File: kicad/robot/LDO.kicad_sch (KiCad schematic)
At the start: 17 parts, among them U14 MAX77642ANA+

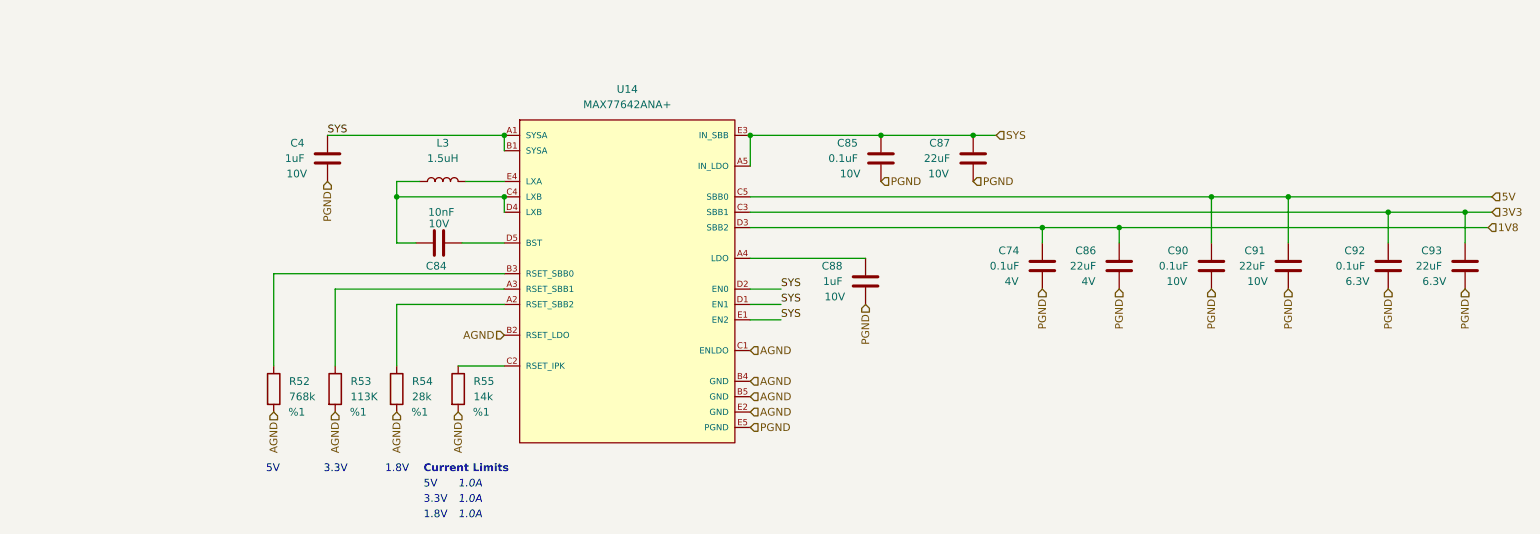
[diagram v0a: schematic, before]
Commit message: Add current breaks between each section of hardware.
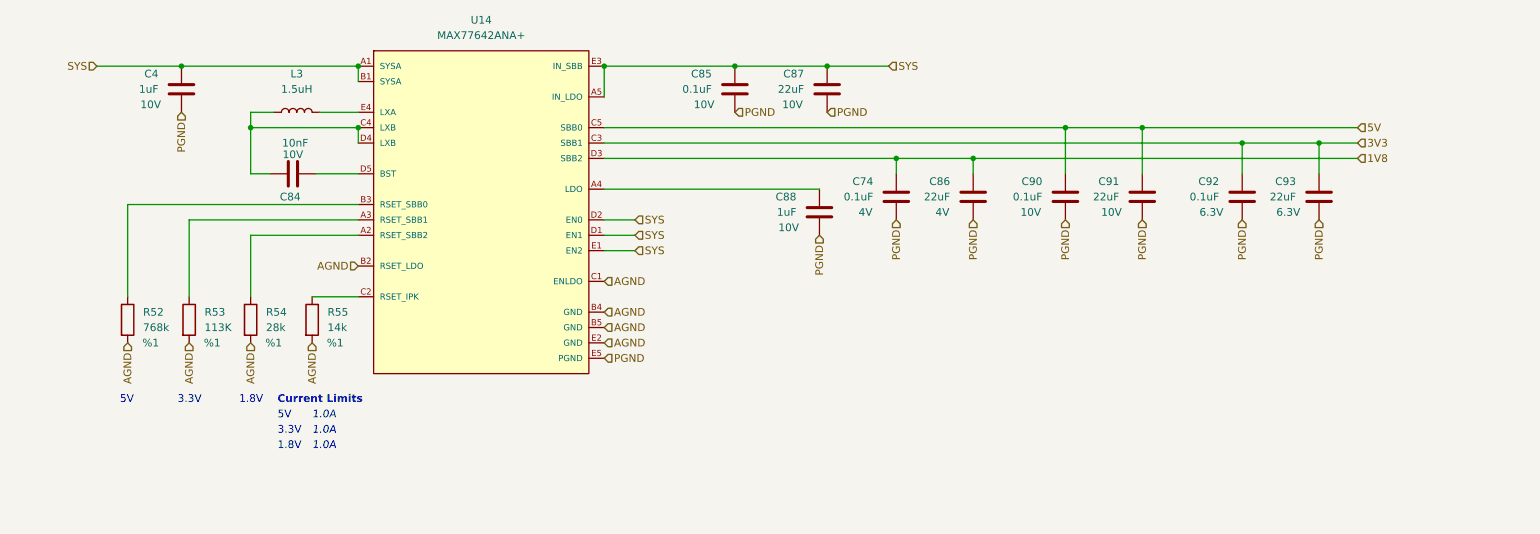
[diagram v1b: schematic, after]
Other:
- moved on the sheet: C4, C74, C84, C85, C86, C87, C88, C90, C91, C92, C93, L3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

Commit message: Add test points for testing current on SIMO. Also add shunt switches to turn on/off each (i.e. on pins D2, D1, and E1).
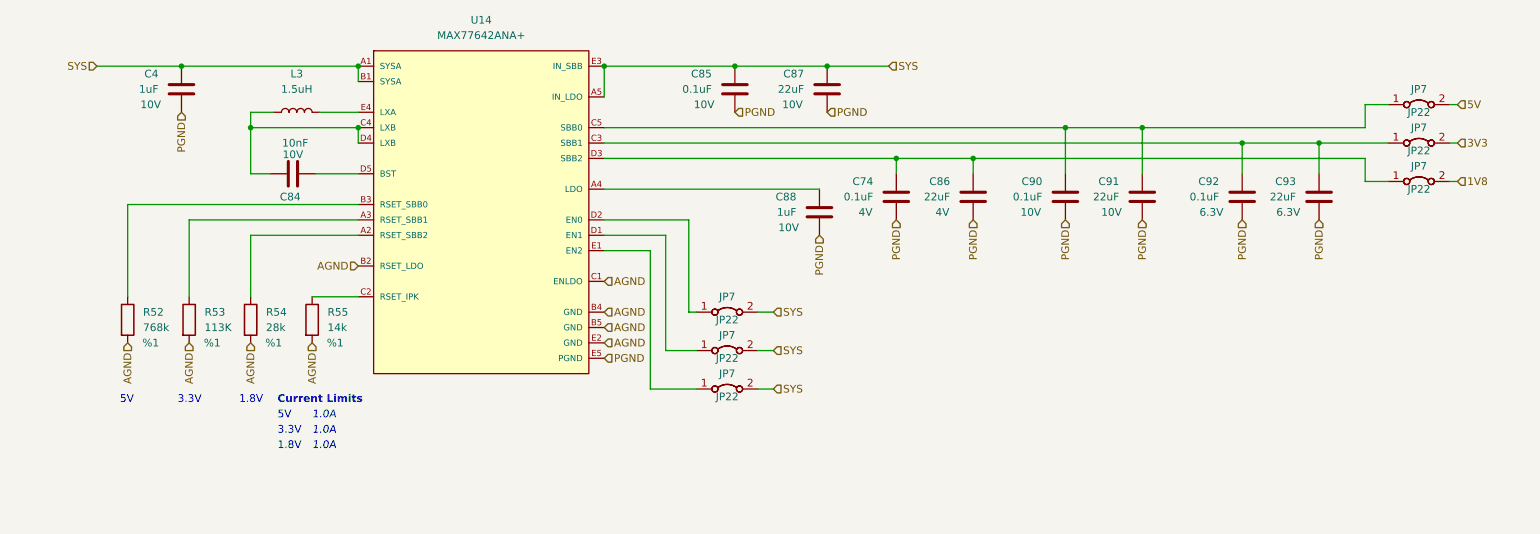
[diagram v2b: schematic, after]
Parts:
- added JP22 (x6): Jumper, custom_connectors:2.54mm_2pointJumper, symbol Jumper:Jumper
- added JP7 (x6): Jumper_Bridged, custom_connectors:2.54mm_2pointJumperClosed, symbol Jumper:Jumper_2_Bridged
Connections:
- net 1V8: now also JP7.2 (B); no longer C74.1, C86.1, U14.D3 (SBB2)
- net 3V3: now also JP7.2 (B); no longer C92.1, C93.1, U14.C3 (SBB1)
- net 5V: now also JP7.2 (B); no longer C90.1, C91.1, U14.C5 (SBB0)
- net SYS: now also JP7.2 (B), JP7.2 (B), JP7.2 (B); no longer U14.D1 (EN1), U14.D2 (EN0), U14.E1 (EN2)
- new net: C92.1, C93.1, JP7.1 (A), U14.C3 (SBB1)
- new net: C74.1, C86.1, JP7.1 (A), U14.D3 (SBB2)
- new net: C90.1, C91.1, JP7.1 (A), U14.C5 (SBB0)
- new net: JP7.1 (A), U14.D1 (EN1)
- new net: JP7.1 (A), U14.D2 (EN0)
- new net: JP7.1 (A), U14.E1 (EN2)

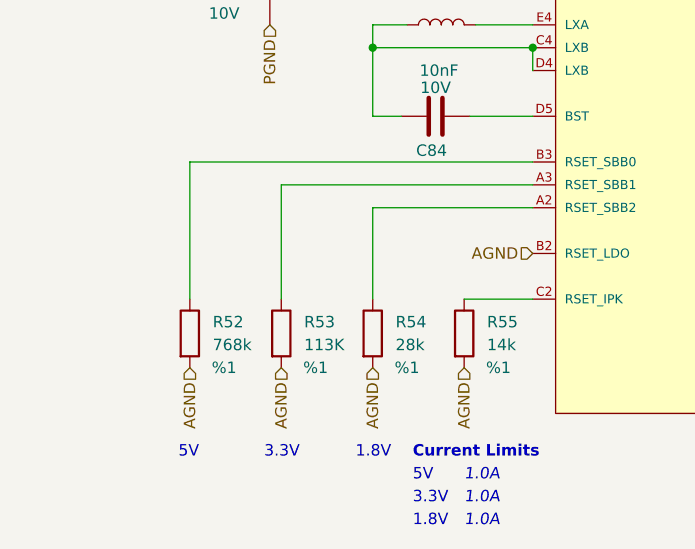
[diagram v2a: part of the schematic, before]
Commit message: Added set resistor for LDO and changed size to 0603 for LDO output capacitor as recommended by datasheet Output Capacitor Selection
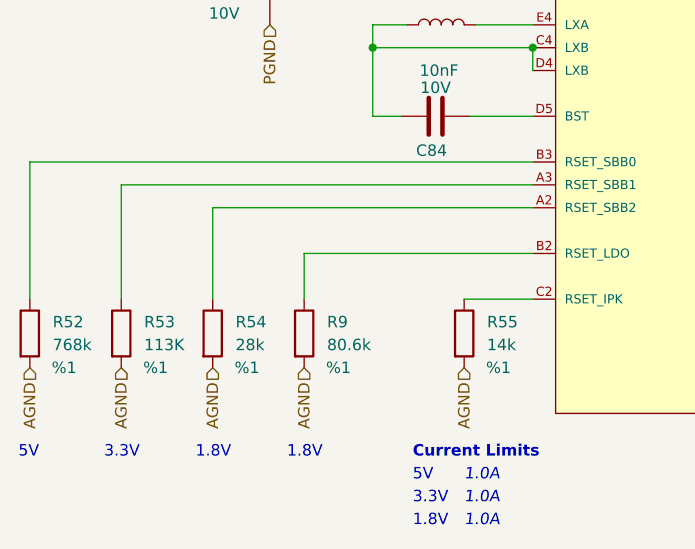
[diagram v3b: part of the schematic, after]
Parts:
- added R9: 80.6k, Resistor_SMD:R_0402_1005Metric, symbol Device:R
- C88: footprint Capacitor_SMD:C_0402_1005Metric -> Capacitor_SMD:C_0603_1608Metric; Manufacturer Murata -> (none); Part Number GRM155R61E105KA12D -> (none)
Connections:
- net AGND: now also R9.2; no longer U14.B2 (RSET_LDO)
- new net: R9.1, U14.B2 (RSET_LDO)
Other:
- moved on the sheet: R52, R53, R54

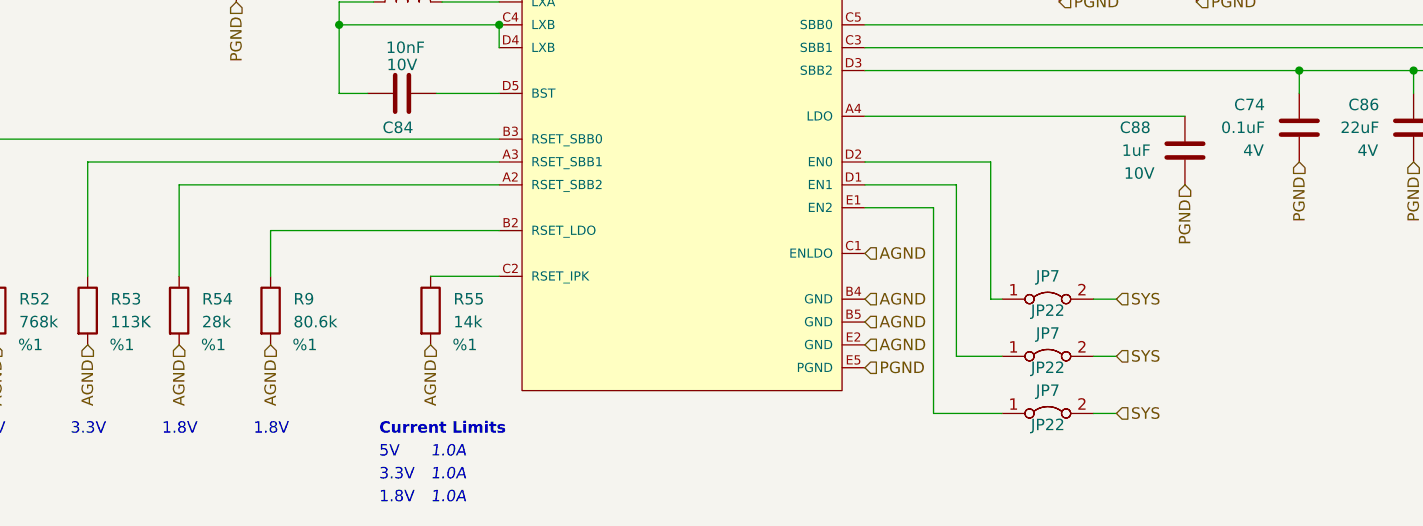
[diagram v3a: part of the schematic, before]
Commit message: Enable LDO and set it at 1.8V and Disable SBB2 and follow recommendations for unused outputs
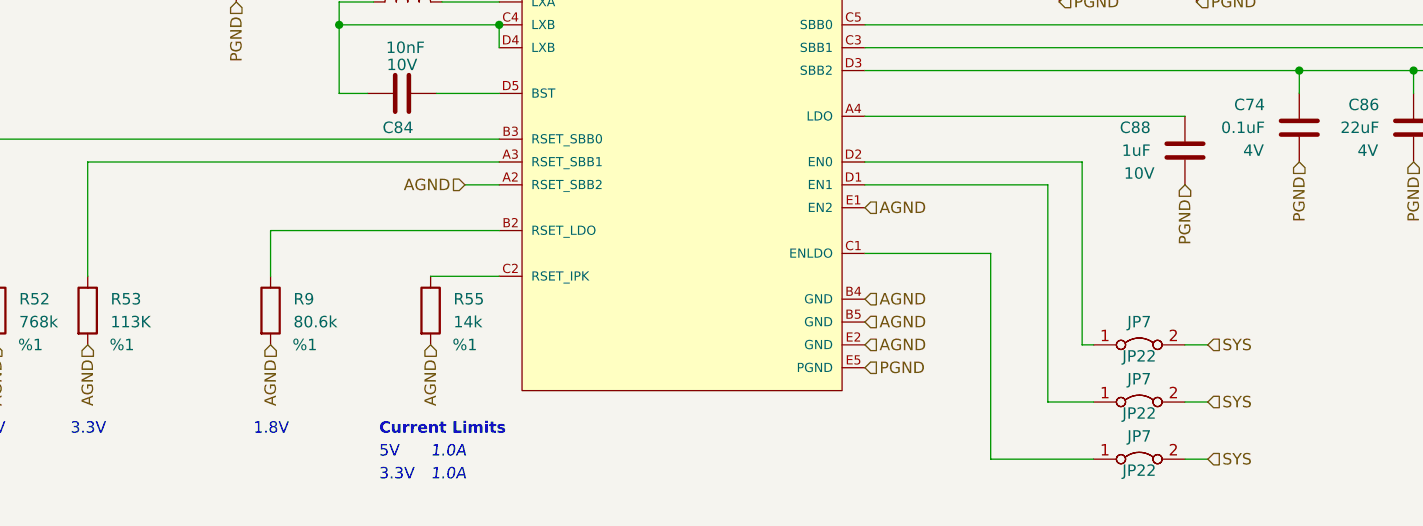
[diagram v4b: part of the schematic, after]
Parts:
- removed R54: 28k, Resistor_SMD:R_0603_1608Metric, symbol Device:R
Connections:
- net AGND: now also U14.A2 (RSET_SBB2), U14.E1 (EN2); no longer U14.C1 (ENLDO)
- net at JP7.1 (A): now also U14.C1 (ENLDO); no longer U14.E1 (EN2)
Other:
- moved on the sheet: JP22, JP7

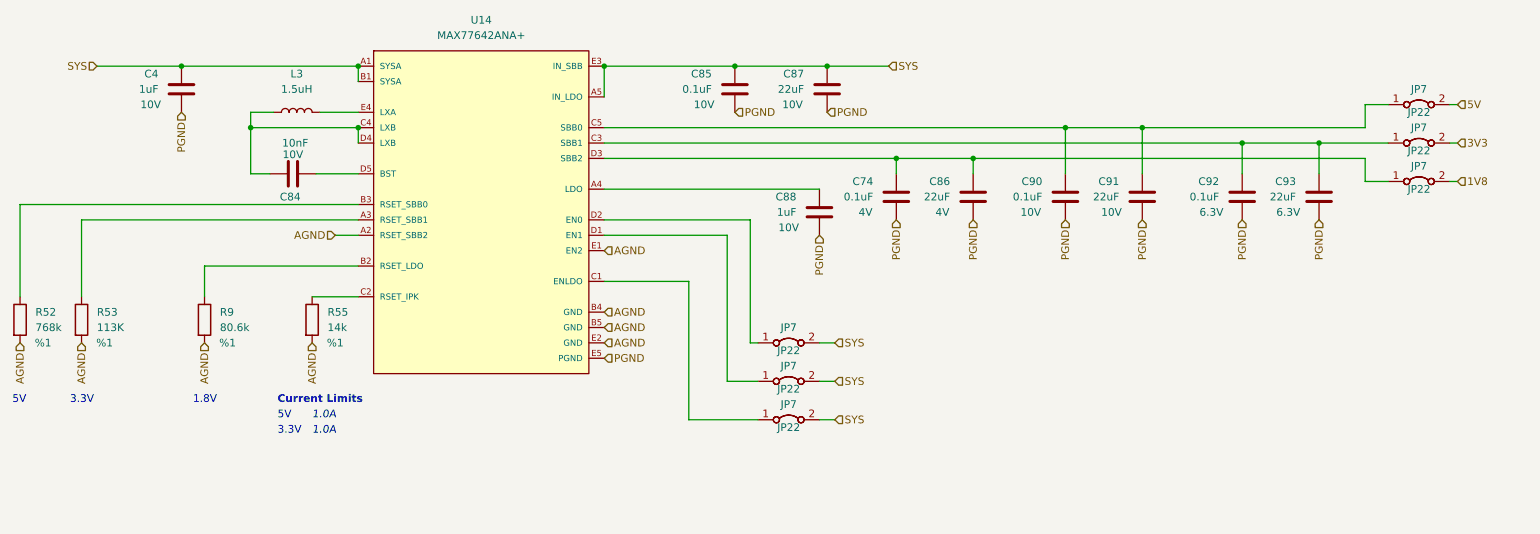
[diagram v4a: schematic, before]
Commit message: Eleminated 5V rail and corrected a few mistakes in SIMO config
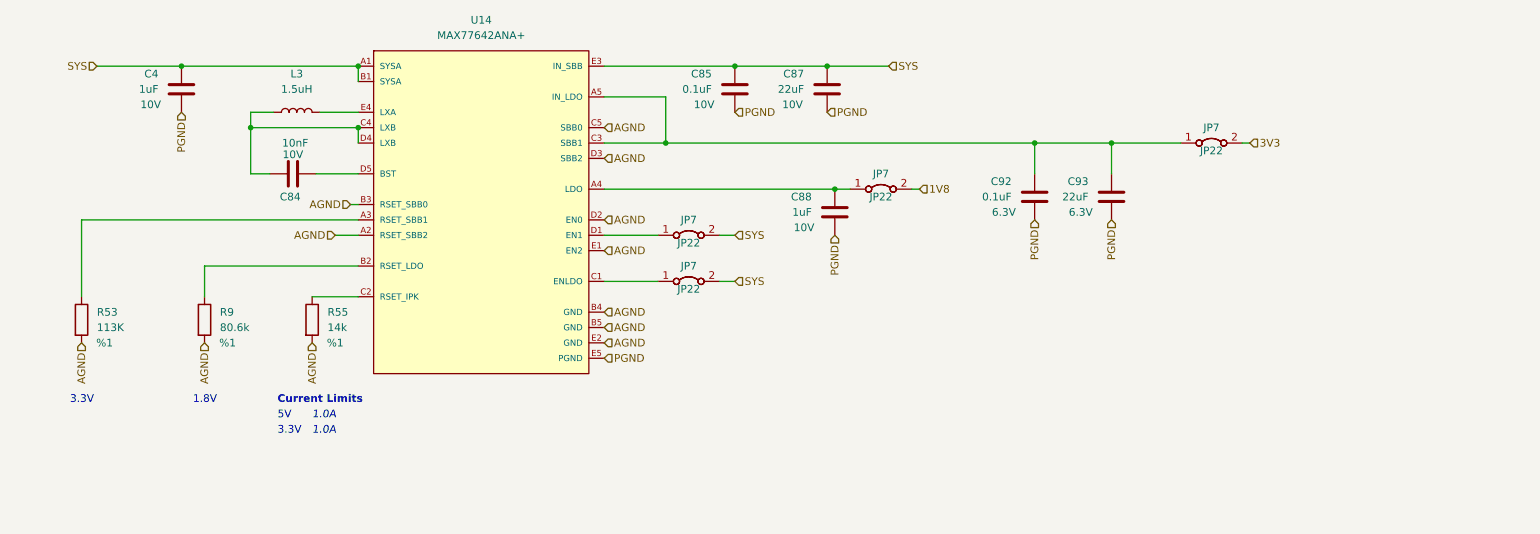
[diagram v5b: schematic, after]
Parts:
- removed C74, C90: 0.1uF, Capacitor_SMD:C_0402_1005Metric, symbol Device:C
- removed C86, C91: 22uF, Capacitor_SMD:C_0603_1608Metric, symbol Device:C
- removed JP22 (x2): Jumper, custom_connectors:2.54mm_2pointJumper, symbol Jumper:Jumper
- removed JP7 (x2): Jumper_Bridged, custom_connectors:2.54mm_2pointJumperClosed, symbol Jumper:Jumper_2_Bridged
- removed R52: 768k, Resistor_SMD:R_0603_1608Metric, symbol Device:R
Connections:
- net AGND: now also U14.B3 (RSET_SBB0), U14.C5 (SBB0), U14.D2 (EN0), U14.D3 (SBB2)
- net SYS: no longer U14.A5 (IN_LDO)
- net at C92.1, C93.1, JP7.1 (A)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: now also U14.A5 (IN_LDO)
- net at C88.1, U14.A4 (LDO): now also JP7.1 (A)
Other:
- moved on the sheet: C88, C92, C93, JP22, JP7

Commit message: updated all footprint fields in schematic symbols with local robot ones
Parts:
- C4, C84, C85, C92: footprint Capacitor_SMD:C_0402_1005Metric -> robot:C_0402_1005Metric
- C87, C88, C93: footprint Capacitor_SMD:C_0603_1608Metric -> robot:C_0603_1608Metric
- JP22: footprint custom_connectors:2.54mm_2pointJumper -> robot:2.54mm_2pointJumper
- JP7: footprint custom_connectors:2.54mm_2pointJumperClosed -> robot:2.54mm_2pointJumperClosed
- L3: footprint custom_inductors:NRS6028T1R5NMGJ -> robot:NRS6028T1R5NMGJ
- R53, R55: footprint Resistor_SMD:R_0603_1608Metric -> robot:R_0603_1608Metric
- R9: footprint Resistor_SMD:R_0402_1005Metric -> robot:R_0402_1005Metric
- U14: footprint Package_BGA:Maxim-N252B2-1-0-A-MFG -> robot:Maxim-N252B2-1-0-A-MFG
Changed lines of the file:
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@@
       (effects (font (size 1.27 1.27)) (justify left))
     )
-    (property "Footprint" "Resistor_SMD:R_0603_1608Metric" (at 24.892 106.68 90)
+    (property "Footprint" "robot:R_0603_1608Metric" (at 24.892 106.68 90)
       (effects (font (size 1.27 1.27)) hide)
     )
@@
       (effects (font (size 1.27 1.27)) (justify left))
     )
-    (property "Footprint" "Capacitor_SMD:C_0603_1608Metric" (at 195.8848 90.17 0)
+    (property "Footprint" "robot:C_0603_1608Metric" (at 195.8848 90.17 0)
       (effects (font (size 1.27 1.27)) hide)
     )
@@
       (effects (font (size 1.27 1.27)) (justify left))
     )
-    (property "Footprint" "Capacitor_SMD:C_0603_1608Metric" (at 150.1648 92.71 0)
+    (property "Footprint" "robot:C_0603_1608Metric" (at 150.1648 92.71 0)
       (effects (font (size 1.27 1.27)) hide)
     )
@@
       (effects (font (size 1.27 1.27)) hide)
     )
-    (property "Footprint" "custom_connectors:2.54mm_2pointJumperClosed" (at 213.36 77.47 0)
+    (property "Footprint" "robot:2.54mm_2pointJumperClosed" (at 213.36 77.47 0)
       (effects (font (size 1.27 1.27)) hide)
     )
@@
       (effects (font (size 1.27 1.27)) (justify left))
     )
-    (property "Footprint" "Resistor_SMD:R_0402_1005Metric" (at 45.212 106.68 90)
+    (property "Footprint" "robot:R_0402_1005Metric" (at 45.212 106.68 90)
       (effects (font (size 1.27 1.27)) hide)
     )
@@
       (effects (font (size 1.27 1.27)) (justify left))
     )
-    (property "Footprint" "Capacitor_SMD:C_0603_1608Metric" (at 148.8948 72.39 0)
+    (property "Footprint" "robot:C_0603_1608Metric" (at 148.8948 72.39 0)
       (effects (font (size 1.27 1.27)) hide)
     )
@@
       (effects (font (size 1.27 1.27)) hide)
     )
-    (property "Footprint" "custom_connectors:2.54mm_2pointJumperClosed" (at 127 100.33 0)
+    (property "Footprint" "robot:2.54mm_2pointJumperClosed" (at 127 100.33 0)
       (effects (font (size 1.27 1.27)) hide)
     )
@@
       (effects (font (size 1.27 1.27)) hide)
     )
-    (property "Footprint" "custom_connectors:2.54mm_2pointJumper" (at 158.75 93.345 0)
+    (property "Footprint" "robot:2.54mm_2pointJumper" (at 158.75 93.345 0)
       (effects (font (size 1.27 1.27)) hide)
     )
@@
       (effects (font (size 1.27 1.27)))
     )
-    (property "Footprint" "custom_inductors:NRS6028T1R5NMGJ" (at 62.23 72.39 0)
+    (property "Footprint" "robot:NRS6028T1R5NMGJ" (at 62.23 72.39 0)
       (effects (font (size 1.27 1.27)) hide)
     )
@@
       (effects (font (size 1.27 1.27)) hide)
     )
-    (property "Footprint" "custom_connectors:2.54mm_2pointJumperClosed" (at 158.75 85.09 0)
+    (property "Footprint" "robot:2.54mm_2pointJumperClosed" (at 158.75 85.09 0)
       (effects (font (size 1.27 1.27)) hide)
     )
@@
       (effects (font (size 1.27 1.27)) hide)
     )
-    (property "Footprint" "custom_connectors:2.54mm_2pointJumper" (at 127 100.965 0)
+    (property "Footprint" "robot:2.54mm_2pointJumper" (at 127 100.965 0)
       (effects (font (size 1.27 1.27)) hide)
     )
@@
       (effects (font (size 1.27 1.27)) hide)
     )
-    (property "Footprint" "custom_connectors:2.54mm_2pointJumper" (at 127 108.585 0)
+    (property "Footprint" "robot:2.54mm_2pointJumper" (at 127 108.585 0)
       (effects (font (size 1.27 1.27)) hide)
     )
@@
       (effects (font (size 1.27 1.27)))
     )
-    (property "Footprint" "Package_BGA:Maxim-N252B2-1-0-A-MFG" (at 69.85 54.61 0)
+    (property "Footprint" "robot:Maxim-N252B2-1-0-A-MFG" (at 69.85 54.61 0)
       (effects (font (size 1.27 1.27)) (justify left) hide)
     )
@@
       (effects (font (size 1.27 1.27)) hide)
     )
-    (property "Footprint" "custom_connectors:2.54mm_2pointJumper" (at 213.36 85.725 0)
+    (property "Footprint" "robot:2.54mm_2pointJumper" (at 213.36 85.725 0)
       (effects (font (size 1.27 1.27)) hide)
     )
@@
       (effects (font (size 1.27 1.27)) (justify left))
     )
-    (property "Footprint" "Capacitor_SMD:C_0402_1005Metric" (at 133.6548 72.39 0)
+    (property "Footprint" "robot:C_0402_1005Metric" (at 133.6548 72.39 0)
       (effects (font (size 1.27 1.27)) hide)
     )
@@
       (effects (font (size 1.27 1.27)) hide)
     )
-    (property "Footprint" "custom_connectors:2.54mm_2pointJumperClosed" (at 127 92.71 0)
+    (property "Footprint" "robot:2.54mm_2pointJumperClosed" (at 127 92.71 0)
       (effects (font (size 1.27 1.27)) hide)
     )
@@
       (effects (font (size 1.27 1.27)) (justify left))
     )
-    (property "Footprint" "Capacitor_SMD:C_0402_1005Metric" (at 42.2148 72.39 0)
+    (property "Footprint" "robot:C_0402_1005Metric" (at 42.2148 72.39 0)
       (effects (font (size 1.27 1.27)) hide)
     )
@@
       (effects (font (size 1.27 1.27)) (justify left))
     )
-    (property "Footprint" "Capacitor_SMD:C_0402_1005Metric" (at 183.1848 90.17 0)
+    (property "Footprint" "robot:C_0402_1005Metric" (at 183.1848 90.17 0)
       (effects (font (size 1.27 1.27)) hide)
     )
@@
       (effects (font (size 1.27 1.27)) (justify left))
     )
-    (property "Footprint" "Resistor_SMD:R_0603_1608Metric" (at 62.992 106.68 90)
+    (property "Footprint" "robot:R_0603_1608Metric" (at 62.992 106.68 90)
       (effects (font (size 1.27 1.27)) hide)
     )
@@
       (effects (font (size 1.27 1.27)) (justify left))
     )
-    (property "Footprint" "Capacitor_SMD:C_0402_1005Metric" (at 65.405 83.5152 0)
-      (effects (font (size 1.27 1.27)) hide)
-    )
+    (property "Footprint" "robot:C_0402_1005Metric" (at 65.405 83.5152 0)
+      (effects (font (size 1.27 1.27)) hide)
+    )
